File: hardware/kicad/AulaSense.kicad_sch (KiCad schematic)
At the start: 22 parts, among them J1 ESP32_DevKitV1_Header_Left, J2 ESP32_DevKitV1_Header_Right, J3 Entrada 5V, J4 Buzzer 5V, Q1 BC337, SW1 SW_Push, SW2 SW_Push, SW3 SW_Push

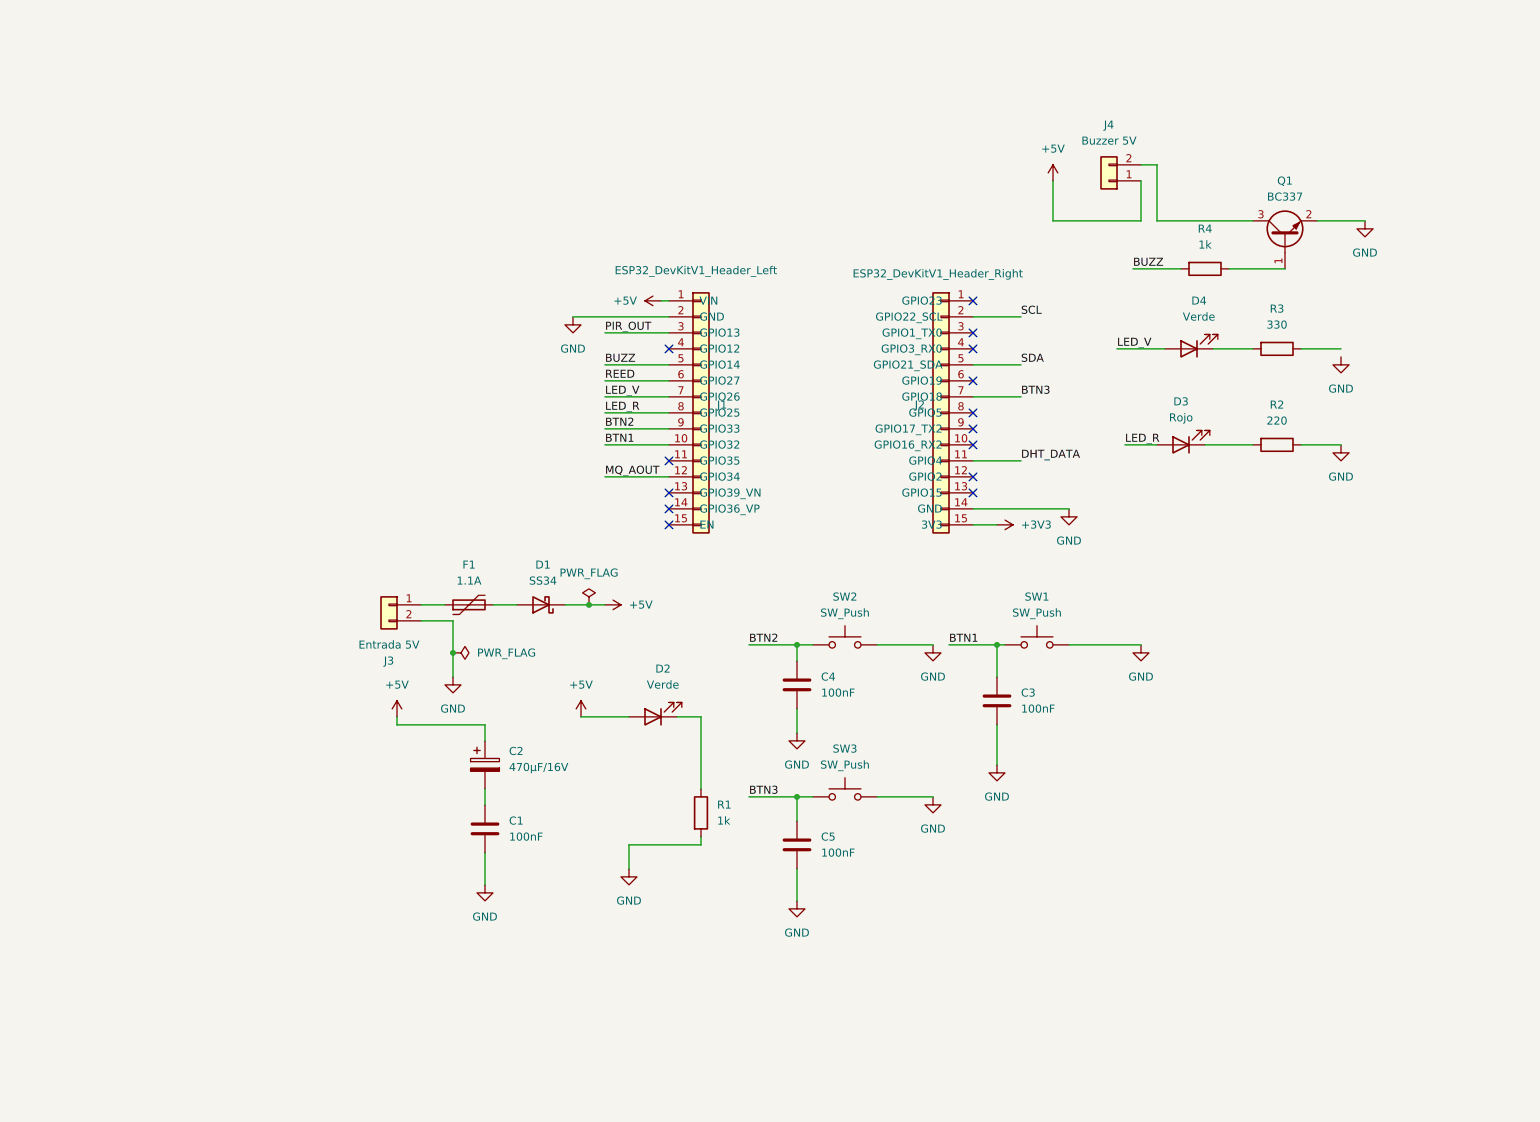
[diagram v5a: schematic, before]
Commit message: feat(hw): conectores de sensores DHT22, PIR y reed
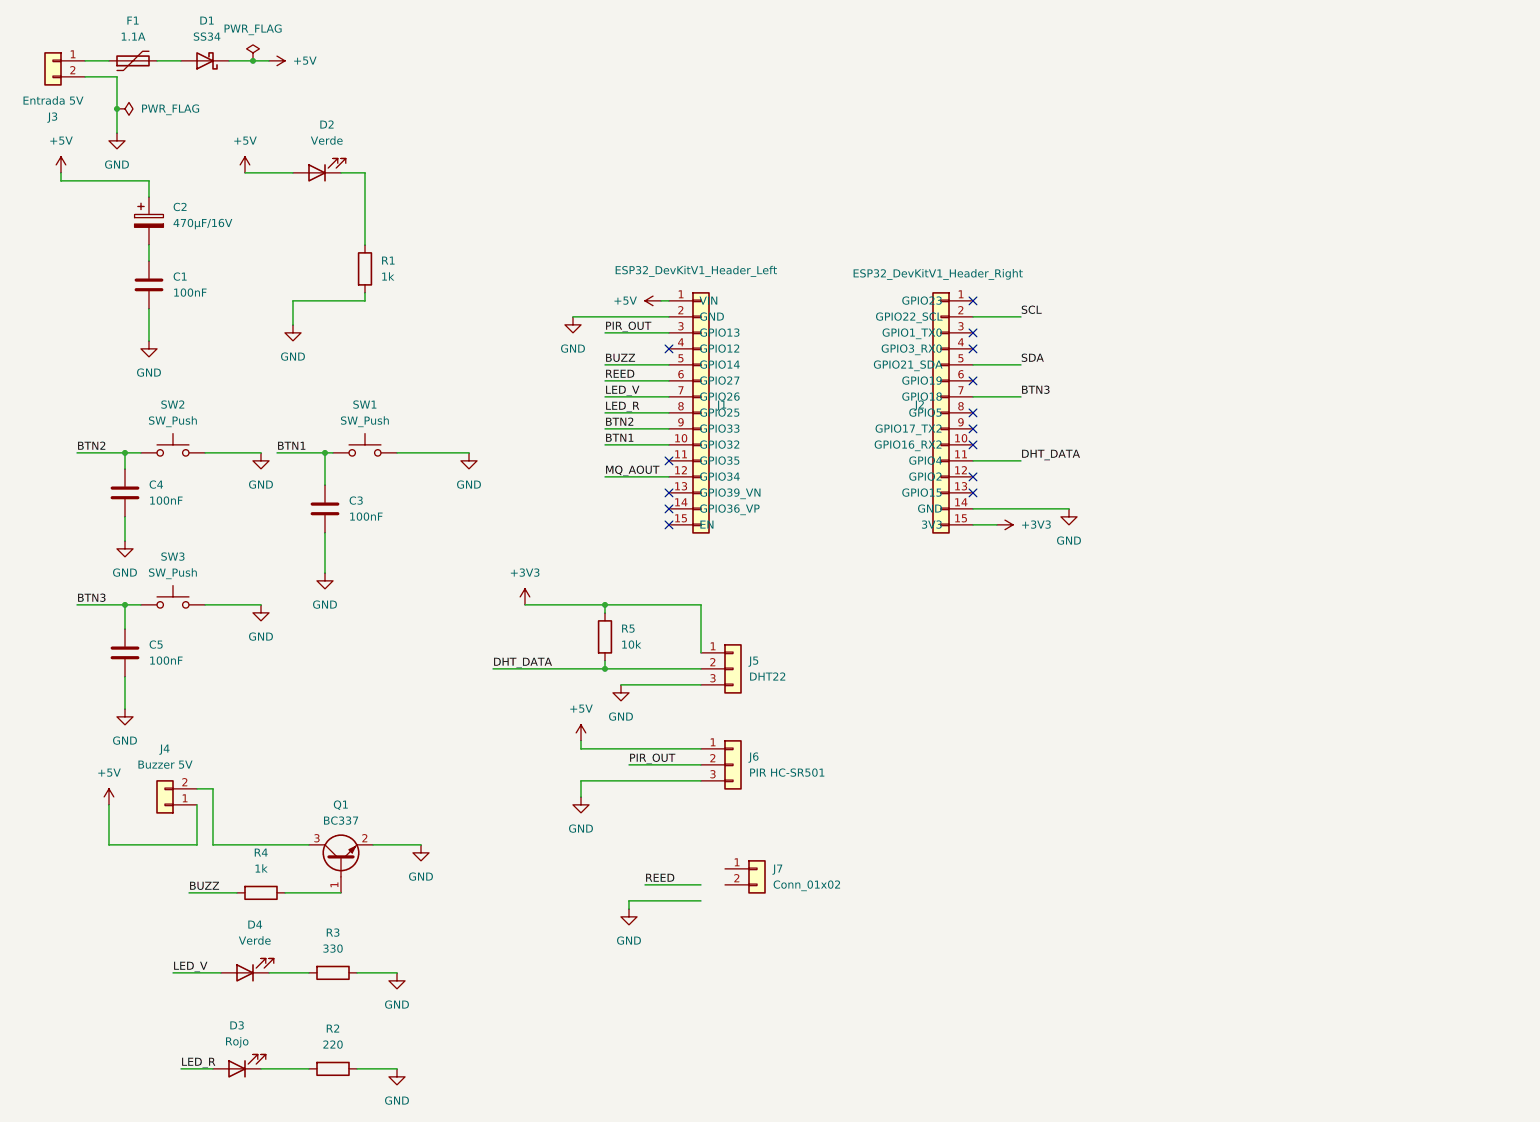
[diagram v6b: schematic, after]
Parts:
- added J5: DHT22, symbol Connector_Generic:Conn_01x03
- added J6: PIR HC-SR501, symbol Connector_Generic:Conn_01x03
- added J7: Conn_01x02, symbol Connector_Generic:Conn_01x02
- added R5: 10k, symbol Device:R
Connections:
- net +3V3: now also J5.1 (Pin_1), R5.1
- net +5V: now also J6.1 (Pin_1)
- net DHT_DATA: now also J5.2 (Pin_2), R5.2
- net GND: now also R3.1, J5.3 (Pin_3), J6.3 (Pin_3)
- net PIR_OUT: now also J6.2 (Pin_2)
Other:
- moved on the sheet: C1, C2, C3, C4, C5, D1, D2, D3, D4, F1, J3, J4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

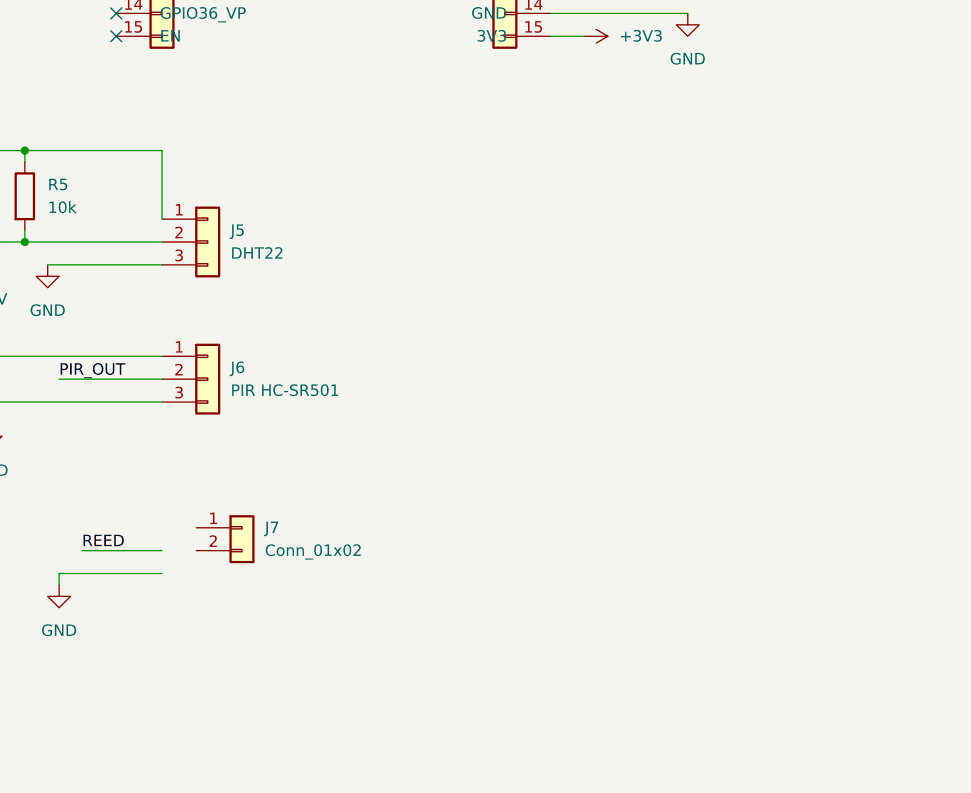
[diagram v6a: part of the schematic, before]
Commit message: feat(hw): bloque MQ-135 con divisor resistivo y filtro
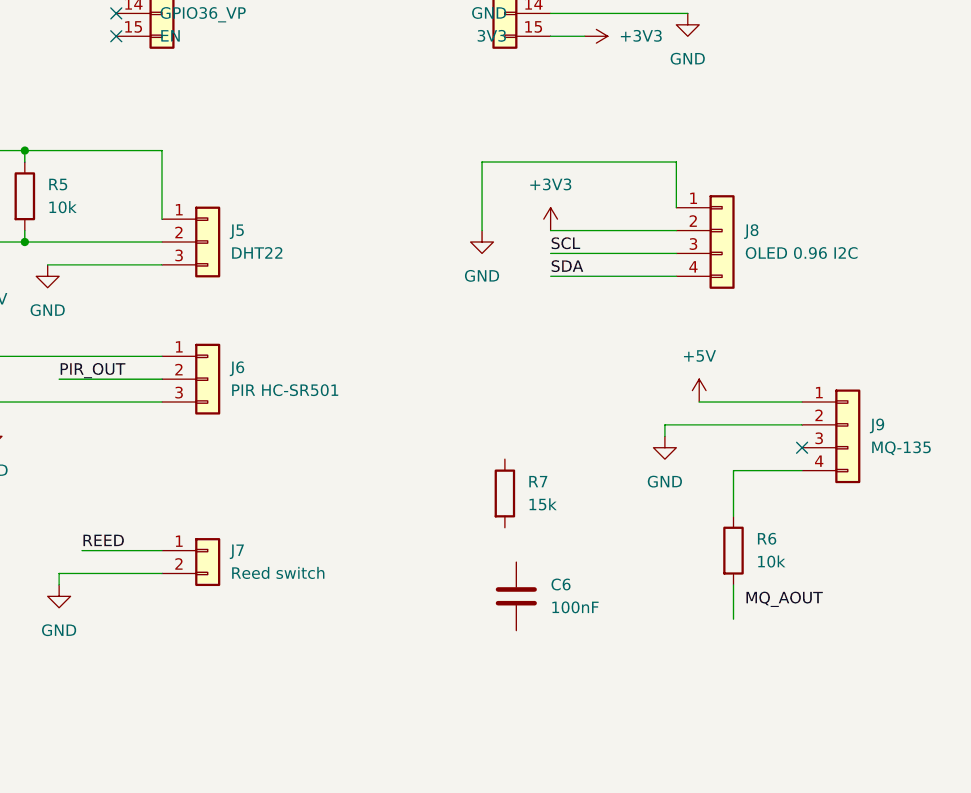
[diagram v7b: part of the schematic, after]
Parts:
- added C6: 100nF, symbol Device:C
- added J8: OLED 0.96 I2C, symbol Connector_Generic:Conn_01x04
- added J9: MQ-135, symbol Connector_Generic:Conn_01x04
- added R6: 10k, symbol Device:R
- added R7: 15k, symbol Device:R
- J7: value Conn_01x02 -> Reed switch
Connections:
- net +3V3: now also J8.2 (Pin_2)
- net +5V: now also J9.1 (Pin_1)
- net GND: now also J7.2 (Pin_2), J8.1 (Pin_1), J9.2 (Pin_2)
- net REED: now also J7.1 (Pin_1)
- net SCL: now also J8.3 (Pin_3)
- net SDA: now also J8.4 (Pin_4)
- new net: J9.4 (Pin_4), R6.1
- no-connect marks 14 -> 15
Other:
- moved on the sheet: J7

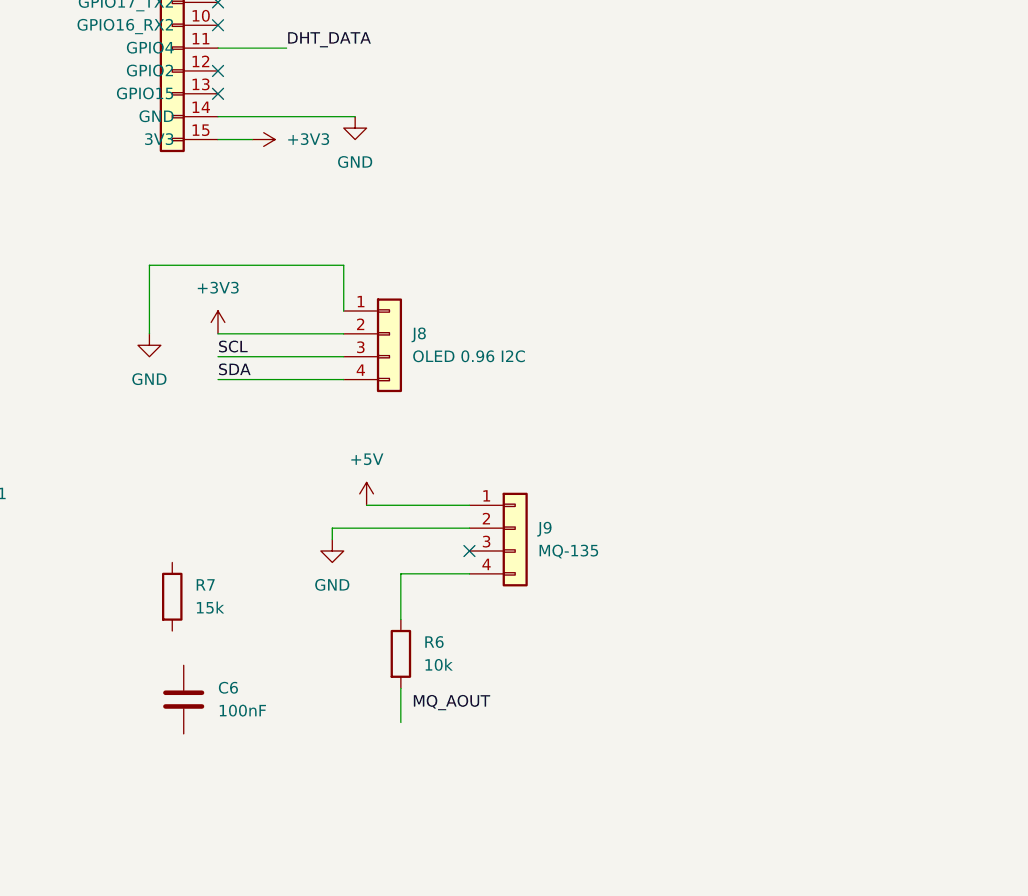
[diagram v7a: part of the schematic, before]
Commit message: feat(hw): esquematico completo con ERC limpio
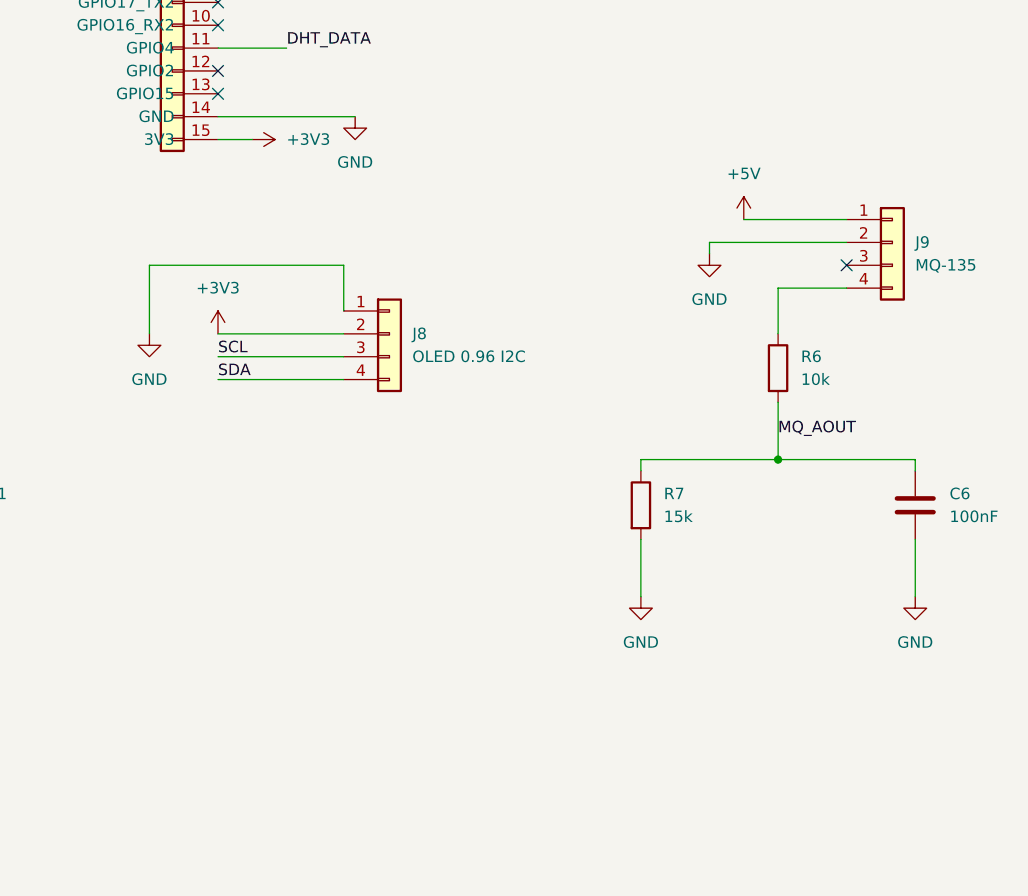
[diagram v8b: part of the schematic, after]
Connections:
- net GND: now also C6.2, R7.2
- net MQ_AOUT: now also C6.1, R6.2, R7.1
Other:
- moved on the sheet: C6, J9, R6, R7
